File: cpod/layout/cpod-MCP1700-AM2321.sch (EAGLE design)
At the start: 12 parts

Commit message: 微调
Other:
- note added: "Arduino Pro Mini (ATMEGA328P 3.3V 8MHz)"
- note added: "Vout = 3.3V"
- note added: "Vraw (3 AA LR6 Batteries) = 4.5V"
- note removed: "Arduino Pro Mini (3.3V 8MHz)"
- moved on the sheet: ARDUINO1, ARDUINO2, I2C

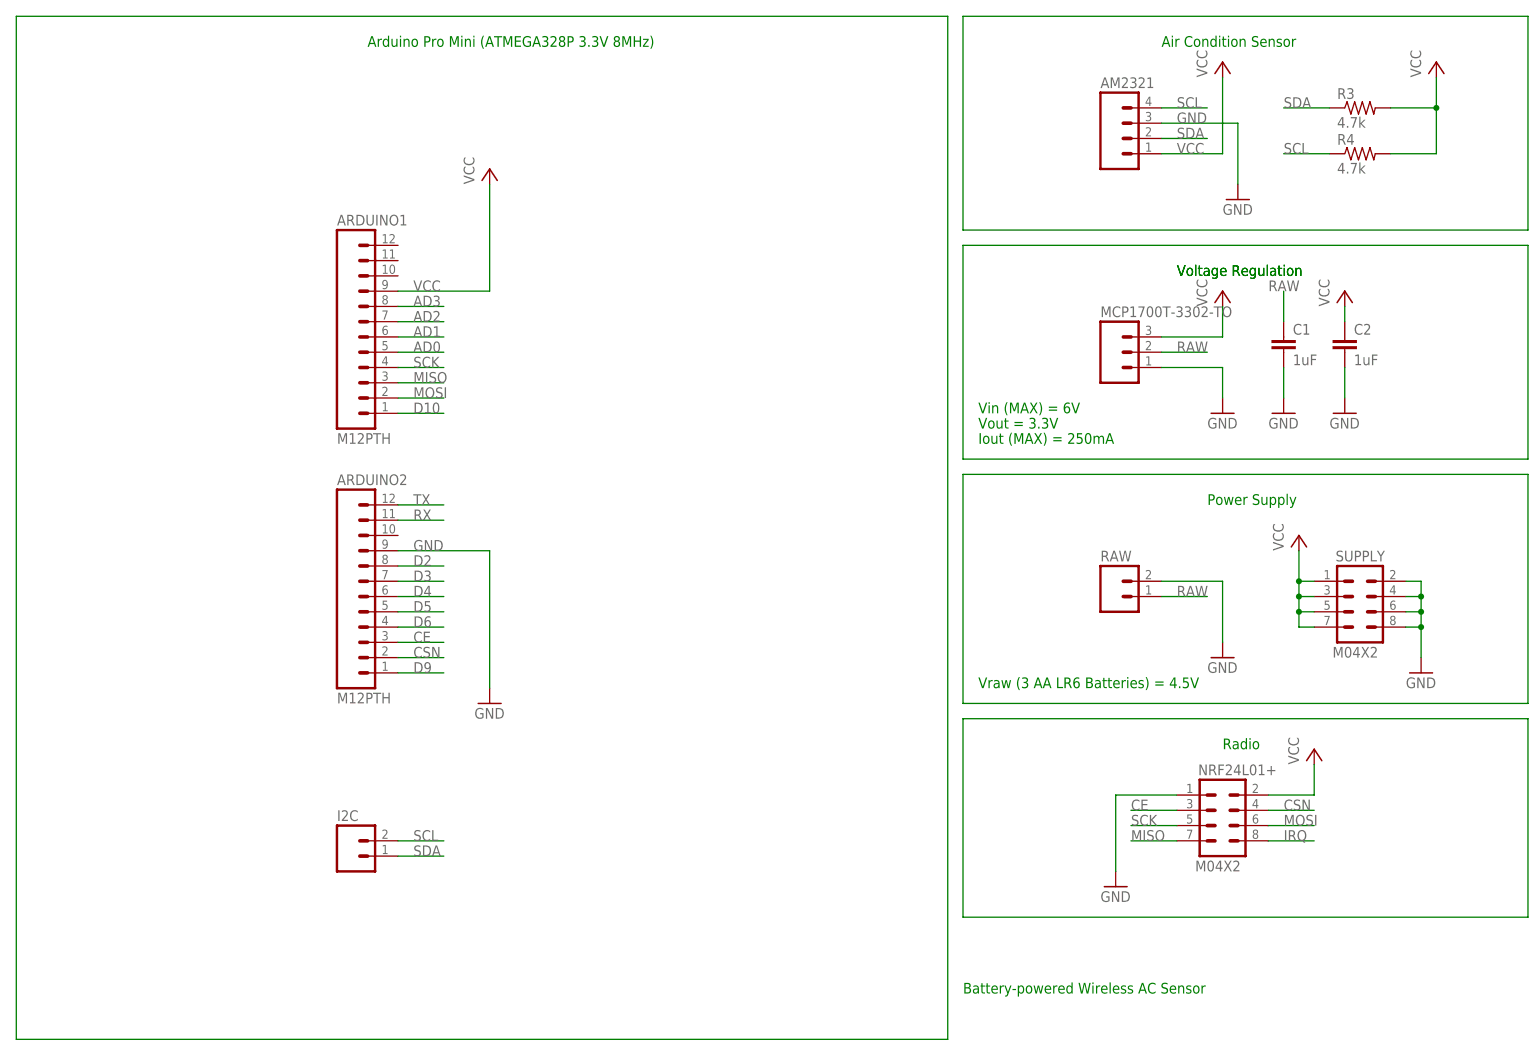
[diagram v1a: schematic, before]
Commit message: 改为单总线
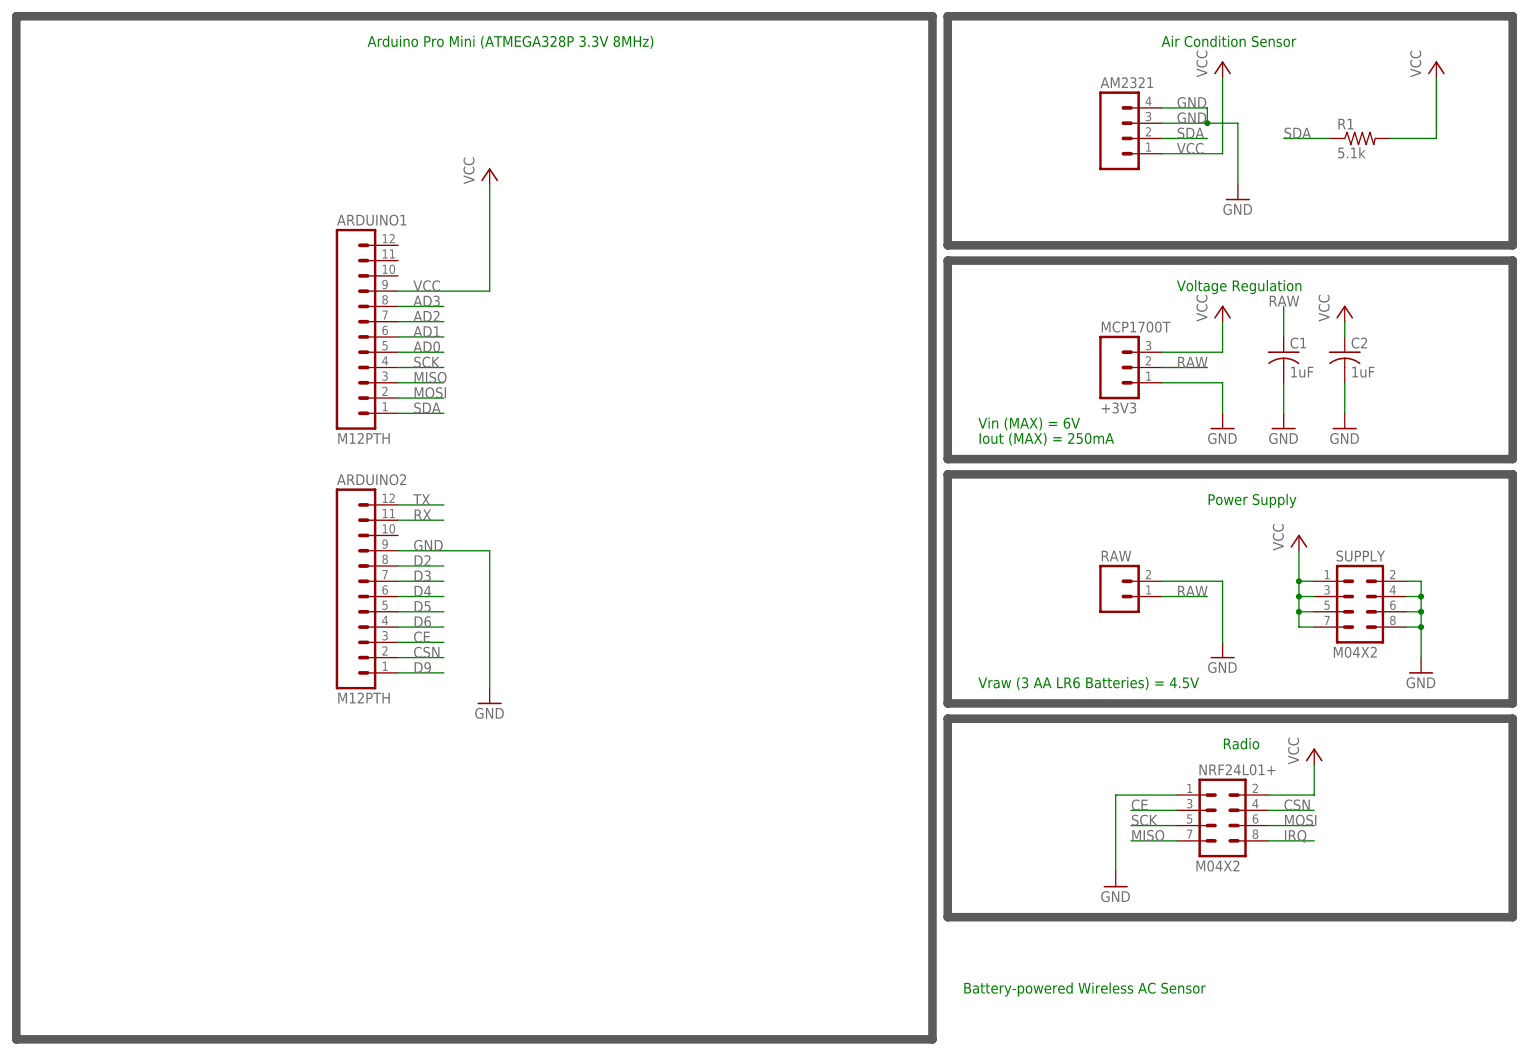
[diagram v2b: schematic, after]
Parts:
- removed I2C: (no value), SparkFun-Connectors:M02PTH
- removed MCP1700T-3302-TO: (no value), SparkFun-Connectors:M03PTH
- removed R3, R4: 4.7k, SparkFun-Resistors:RESISTORAXIAL-0.3
- added MCP1700T: +3V3, SparkFun-Connectors:M03PTH
- added R1: 5.1k, rcl:R-US_0204/2V
- C1, C2: device SparkFun-Capacitors:CAPPTH -> rcl:C-US025-024X044
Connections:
- removed net D10: ARDUINO1.1
- removed net SCL: AM2321.4, I2C.2, R4.1
- net GND: now also AM2321.4, MCP1700T.1; no longer MCP1700T-3302-TO.1
- net RAW: now also MCP1700T.2; no longer MCP1700T-3302-TO.2
- net SDA: now also ARDUINO1.1, R1.1; no longer I2C.1, R3.1
- net VCC: now also MCP1700T.3, R1.2; no longer MCP1700T-3302-TO.3, R3.2, R4.2
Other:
- note removed: "Vout = 3.3V"
- moved on the sheet: C1, C2

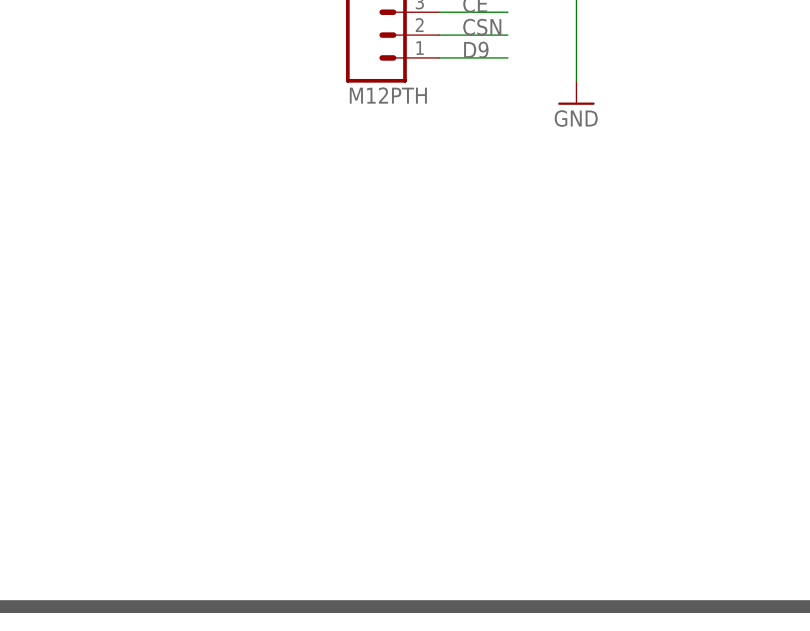
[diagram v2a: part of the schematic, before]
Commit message: 增加了DS1302
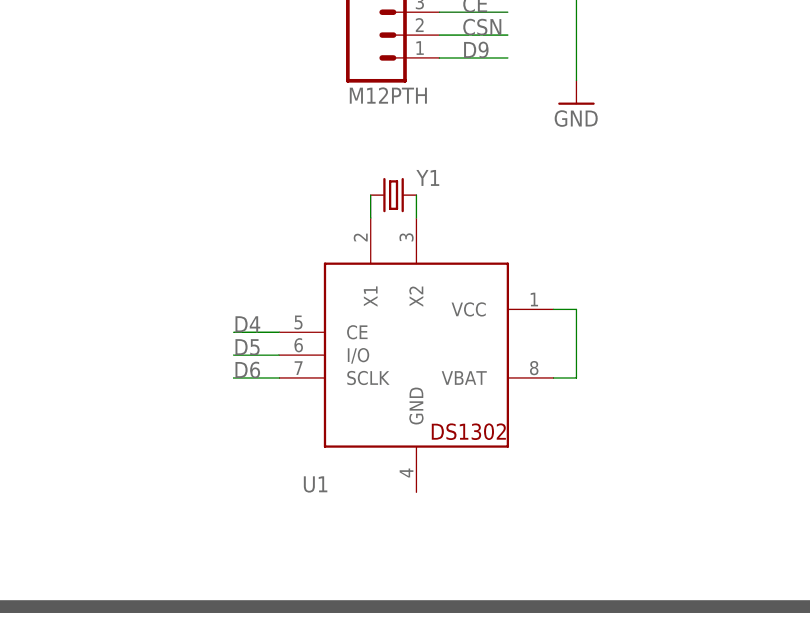
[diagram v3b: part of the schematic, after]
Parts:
- added U1: DS1302, adafruit-maxim:DS1302
- added Y1: (no value), SparkFun-FreqCtrl:CRYSTALTC26H
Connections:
- new net N$1: U1.X1, Y1.1
- new net N$2: U1.X2, Y1.2
- new net N$3: U1.VBAT, U1.VCC
- net D4: now also U1.CE
- net D5: now also U1.I/O
- net D6: now also U1.SCLK
